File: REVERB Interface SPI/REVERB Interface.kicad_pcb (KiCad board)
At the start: 2 copper layers, 90.2 x 95.9 mm, 62 parts, among them J1 RPiZeroW, J2 Iridium, J3 APRS, J4 Antenna, M1 MountingHole_Pad, M2 MountingHole_Pad, M3 MountingHole_Pad, M4 MountingHole_Pad, M5 PiMount, M6 PiMount, M7 PiMount, M8 PiMount, U1 LSM9DS1BOB, U2 MAX3232, U3 SC16IS752IPW, U4 TXB0104D, Y1 1.8432MHz

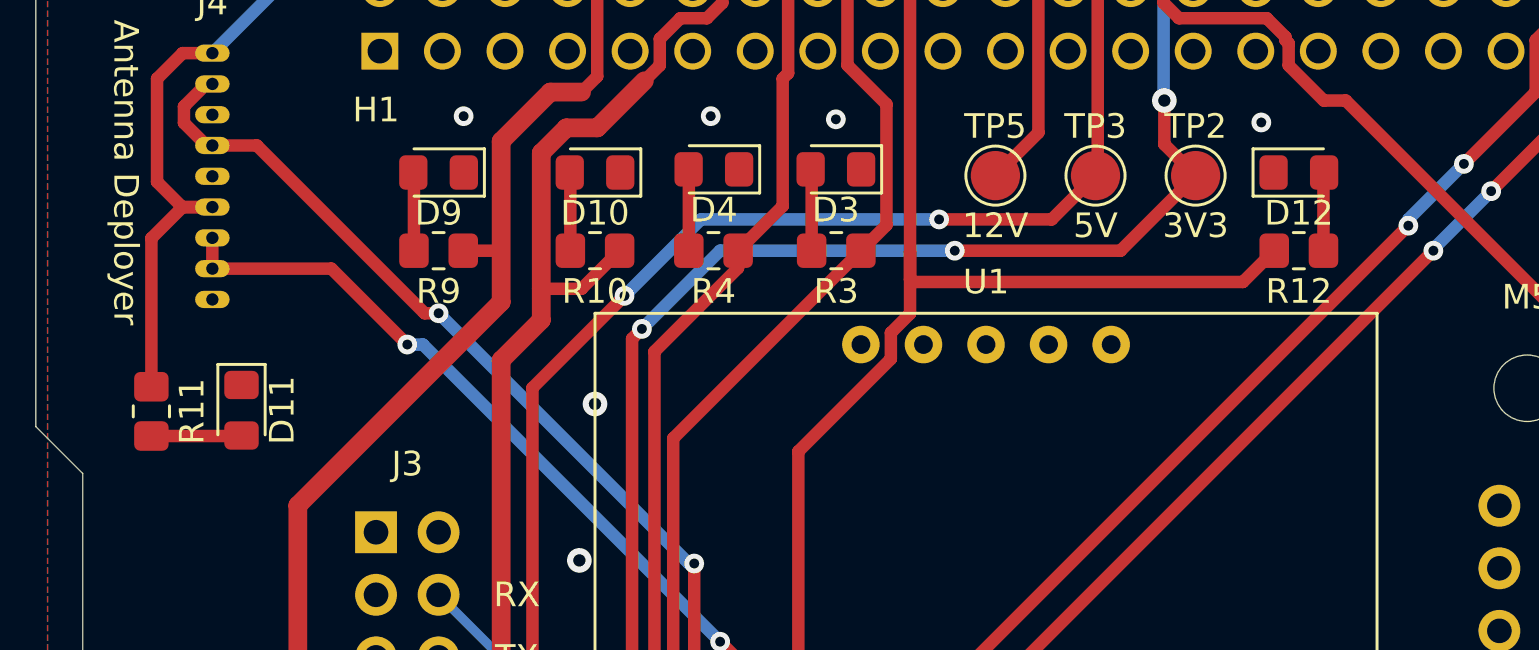
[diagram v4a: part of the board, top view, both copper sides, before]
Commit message: add switch led silkscreen labels
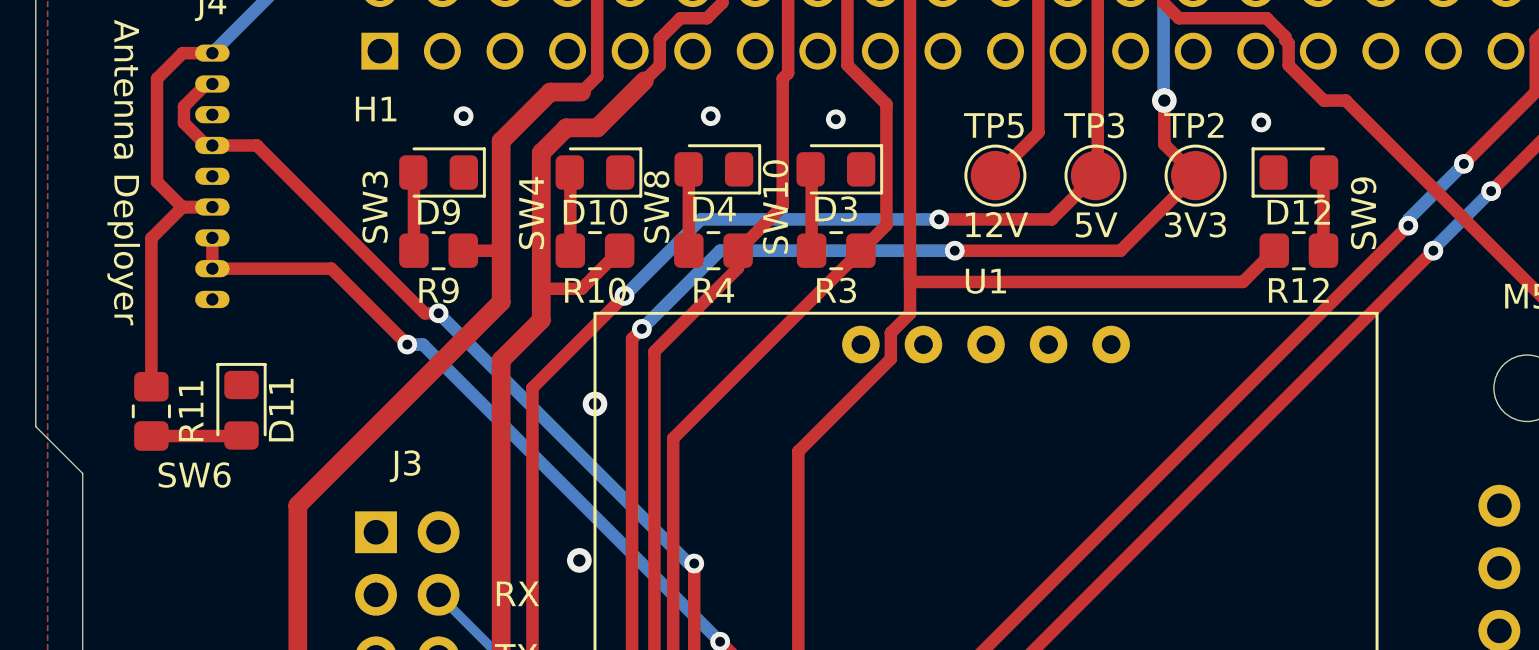
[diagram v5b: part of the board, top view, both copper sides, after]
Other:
- board text added: "SW10"
- board text added: "SW3"
- board text added: "SW4"
- board text added: "SW6"
- board text added: "SW8"
- board text added: "SW9"
